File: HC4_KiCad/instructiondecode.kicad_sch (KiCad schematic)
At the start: 57 parts, among them IC10 74HC4002, IC18 74HC32, IC19 74HC74, IC20 74HC00, IC21 74HC4053, IC22 74HC04, IC23 74HC151

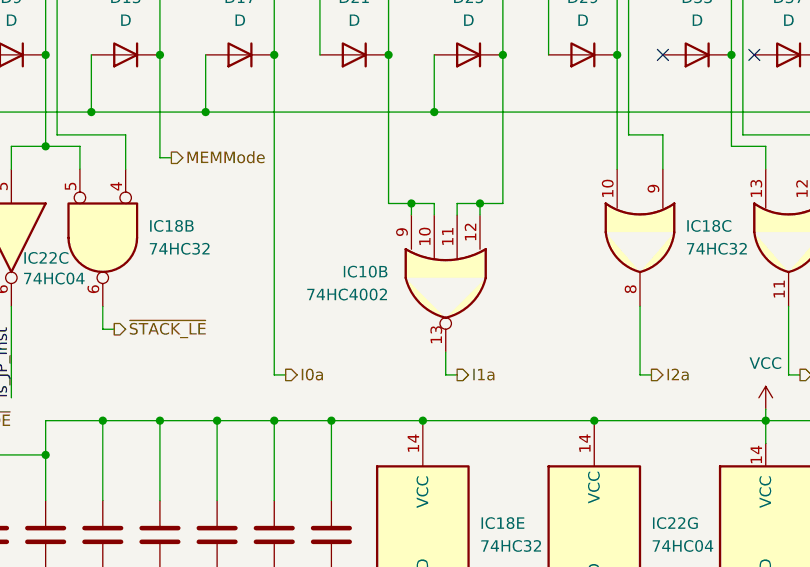
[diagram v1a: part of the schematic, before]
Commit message: とりあえずIC配置確定
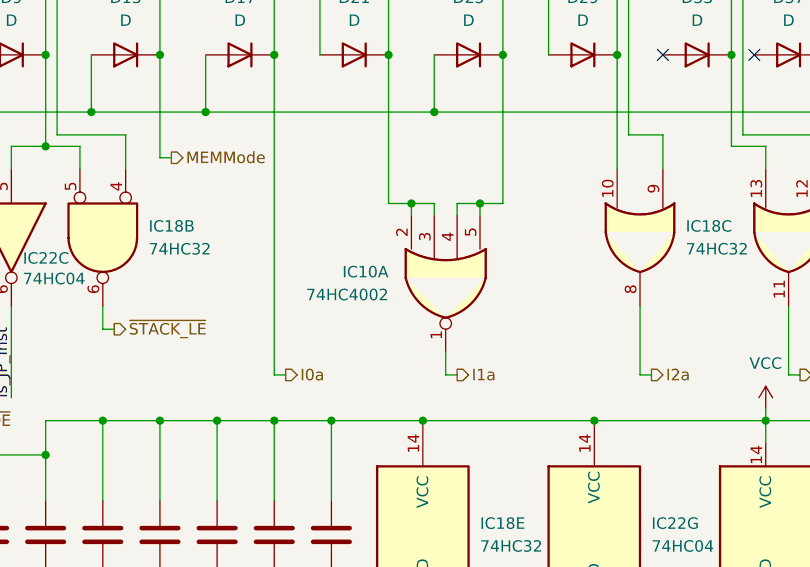
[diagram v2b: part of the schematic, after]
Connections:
- net I1a: now also IC10.1; no longer IC10.13
- net at D18.1 (K), D19.1 (K), D20.1 (K)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: now also IC10.2, IC10.3; no longer IC10.10, IC10.9
- net at D22.1 (K), D23.1 (K), D24.1 (K)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: now also IC10.4, IC10.5; no longer IC10.11, IC10.12
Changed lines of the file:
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@@
 		(at 205.74 120.65 90)
 		(mirror x)
-		(unit 2)
+		(unit 1)
 		(exclude_from_sim no)
 		(in_bom yes)
@@
 				(path "/33731ded-38c0-4297-bdd8-92b082f46ff8/164b1f41-83dc-48ee-8dfe-457b556a7022"
 					(reference "IC10")
-					(unit 2)
+					(unit 1)
 				)
 			)

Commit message: またも手直し
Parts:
- renumbered RN6 to RN8
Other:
- title: CPU -> HC4_CPU

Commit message: 回路の改良　試験は明日やる
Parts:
- removed unit 4 of IC20
- removed unit 3 of IC20
- removed unit 4 of IC22
- removed RN8: 10k, Resistor_THT:R_Array_SIP9, symbol Device:R_Network08_Split
- added unit 4 of IC20
- added unit 3 of IC21
- added unit 4 of IC21
- added RN7: 10k, Resistor_THT:R_Array_SIP9, symbol Device:R_Network08_Split
- D10, D11, D12, D13, D14, D15, D16, D17, D18, D19, D2, D20, D21, D22, D23, D24, D25, D26, D27, D28, D29, D3, D30, D31, D32, D33, D34, D35, D36, D37, D38, D39, D4, D40, D41, D5, D6, D7, D8, D9: footprint Library:DO-35_horizontal_anodeup_Smallhole -> Diode_SMD:D_SOD-323_HandSoldering
- renumbered IC19 to IC18, IC18 to IC19, IC22 to IC20, IC20 to IC21, IC21 to IC22
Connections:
- net ALU_~{Eb}: now also IC21.11
- net I0a: now also D14.2 (A), D15.2 (A), D16.2 (A), D17.2 (A), RN7.5 (R4.2); no longer D14.1 (K), D15.1 (K), D16.1 (K), D17.1 (K)
- net Instruction_0: no longer IC22.10 (B)
- net Instruction_4: now also D21.1 (K), D29.1 (K); no longer D21.2 (A), D29.2 (A)
- net Instruction_5: now also D24.1 (K), D32.1 (K), D4.1 (K), D8.1 (K); no longer D20.2 (A), D24.2 (A), D32.2 (A), D4.2 (A), D8.2 (A)
- net Instruction_6: now also D15.1 (K), D23.1 (K), D31.1 (K), D7.1 (K); no longer D15.2 (A), D23.2 (A), D31.2 (A), D7.2 (A)
- net LevelC_OE: now also D38.2 (A), D39.2 (A), D40.2 (A), D41.2 (A); no longer D38.1 (K), D39.1 (K), D40.1 (K), D41.1 (K)
- net MEMMode: now also D10.2 (A), D11.2 (A), D12.2 (A), D13.2 (A), RN7.4 (R3.2); no longer D10.1 (K), D11.1 (K), D12.1 (K), D13.1 (K)
- net READ: now also D34.2 (A), D35.2 (A), D36.2 (A), D37.2 (A); no longer D34.1 (K), D35.1 (K), D36.1 (K), D37.1 (K)
- net VCC: now also IC20.9, RN7.1 (R1), RN7.1 (R1), RN7.1 (R1), RN7.1 (R1), RN7.1 (R1), RN7.1 (R1), RN7.1 (R1), RN7.1 (R1)
- net ~{ALU_OE}: now also D34.1 (K), D6.1 (K), IC22.10 (B), IC21.10; no longer D2.2 (A), D34.2 (A), D6.2 (A)
- net ~{Imm_OE}: now also IC21.8
- net ~{i4}: now also D13.1 (K), D17.1 (K), D25.1 (K); no longer D13.2 (A), D17.2 (A), D25.2 (A)
- net ~{i5}: now also D12.1 (K), D16.1 (K), D36.1 (K), D40.1 (K); no longer D12.2 (A), D16.2 (A), D36.2 (A), D40.2 (A)
- net ~{i6}: now also D11.1 (K), D19.1 (K), D27.1 (K), D3.1 (K), D35.1 (K), D39.1 (K); no longer D11.2 (A), D19.2 (A), D27.2 (A), D3.2 (A), D35.2 (A), D39.2 (A)
- net ~{i7}: now also IC21.13
- net at D33.2 (A): now also D30.2 (A), D31.2 (A), D32.2 (A), IC19.13, RN7.9 (R8.2)
- net at D26.2 (A): now also D27.2 (A), D28.2 (A), D29.2 (A), IC19.10, RN7.8 (R7.2)
- net at D5.2 (A): now also D2.2 (A), D3.2 (A), D4.2 (A), IC21.12, IC21.9, RN7.2 (R1.2)
- net at D18.2 (A): now also D19.2 (A), D20.2 (A), D21.2 (A), IC10.2, IC10.3, RN7.6 (R5.2)
- net at D22.2 (A): now also D23.2 (A), D24.2 (A), D25.2 (A), IC10.4, IC10.5, RN7.7 (R6.2)
- net at D9.2 (A): now also D6.2 (A), D7.2 (A), D8.2 (A), IC19.5, IC20.5, RN7.3 (R2.2)
- now unconnected: D18.1 (K), D2.1 (K), D20.1 (K), D22.1 (K), D26.1 (K), D28.1 (K), D30.1 (K), D33.1 (K), D5.1 (K), D9.1 (K)
- no-connect marks 19 -> 21
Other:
- moved on the sheet: D10, D11, D12, D13, D14, D15, D16, D17, D18, D19, D2, D20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

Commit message: フットプリントをSOPに変更
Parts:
- CP17, CP18, CP19, CP20, CP21, CP22, CP23: footprint Capacitor_THT:C_Disc_D3.0mm_W1.6mm_P2.50mm -> Capacitor_SMD:C_0603_1608Metric
- IC10, IC18, IC19, IC20, IC21: footprint Package_DIP:DIP-14_W7.62mm_Socket -> Package_SO:SO-14_5.3x10.2mm_P1.27mm
- IC22, IC23: footprint Package_DIP:DIP-16_W7.62mm_Socket -> Package_SO:SO-16_5.3x10.2mm_P1.27mm
- R5, R6: footprint Resistor_THT:R_Axial_DIN0207_L6.3mm_D2.5mm_P7.62mm_Horizontal -> Resistor_SMD:R_0603_1608Metric
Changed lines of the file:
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@@
 			)
 		)
-		(property "Footprint" "Package_DIP:DIP-14_W7.62mm_Socket"
+		(property "Footprint" "Package_SO:SO-14_5.3x10.2mm_P1.27mm"
 			(at 69.85 45.72 0)
 			(effects
@@
 			)
 		)
-		(property "Footprint" "Capacitor_THT:C_Disc_D3.0mm_W1.6mm_P2.50mm"
+		(property "Footprint" "Capacitor_SMD:C_0603_1608Metric"
 			(at 181.3052 152.4 0)
 			(effects
@@
 			)
 		)
-		(property "Footprint" "Package_DIP:DIP-14_W7.62mm_Socket"
+		(property "Footprint" "Package_SO:SO-14_5.3x10.2mm_P1.27mm"
 			(at 118.11 63.5 0)
 			(effects
@@
 			)
 		)
-		(property "Footprint" "Capacitor_THT:C_Disc_D3.0mm_W1.6mm_P2.50mm"
+		(property "Footprint" "Capacitor_SMD:C_0603_1608Metric"
 			(at 187.6552 152.4 0)
 			(effects
@@
 			)
 		)
-		(property "Footprint" "Package_DIP:DIP-14_W7.62mm_Socket"
+		(property "Footprint" "Package_SO:SO-14_5.3x10.2mm_P1.27mm"
 			(at 273.05 148.59 0)
 			(effects
@@
 			)
 		)
-		(property "Footprint" "Package_DIP:DIP-14_W7.62mm_Socket"
+		(property "Footprint" "Package_SO:SO-14_5.3x10.2mm_P1.27mm"
 			(at 104.14 133.35 0)
 			(effects
@@
 			)
 		)
-		(property "Footprint" "Capacitor_THT:C_Disc_D3.0mm_W1.6mm_P2.50mm"
+		(property "Footprint" "Capacitor_SMD:C_0603_1608Metric"
 			(at 168.6052 152.4 0)
 			(effects
@@
 			)
 		)
-		(property "Footprint" "Package_DIP:DIP-14_W7.62mm_Socket"
+		(property "Footprint" "Package_SO:SO-14_5.3x10.2mm_P1.27mm"
 			(at 149.86 121.92 0)
 			(effects
@@
 			)
 		)
-		(property "Footprint" "Package_DIP:DIP-14_W7.62mm_Socket"
+		(property "Footprint" "Package_SO:SO-14_5.3x10.2mm_P1.27mm"
 			(at 261.62 148.59 0)
 			(effects
@@
 			)
 		)
-		(property "Footprint" "Package_DIP:DIP-14_W7.62mm_Socket"
+		(property "Footprint" "Package_SO:SO-14_5.3x10.2mm_P1.27mm"
 			(at 241.3 148.59 0)
 			(effects
@@
 			)
 		)
-		(property "Footprint" "Package_DIP:DIP-14_W7.62mm_Socket"
+		(property "Footprint" "Package_SO:SO-14_5.3x10.2mm_P1.27mm"
 			(at 118.11 82.55 0)
 			(effects
@@
 			)
 		)
-		(property "Footprint" "Package_DIP:DIP-14_W7.62mm_Socket"
+		(property "Footprint" "Package_SO:SO-14_5.3x10.2mm_P1.27mm"
 			(at 118.11 101.6 0)
 			(effects
@@
 			)
 		)
-		(property "Footprint" "Package_DIP:DIP-16_W7.62mm_Socket"
+		(property "Footprint" "Package_SO:SO-16_5.3x10.2mm_P1.27mm"
 			(at 130.81 163.83 0)
 			(effects
@@
 			)
 		)
-		(property "Footprint" "Package_DIP:DIP-14_W7.62mm_Socket"
+		(property "Footprint" "Package_SO:SO-14_5.3x10.2mm_P1.27mm"
 			(at 29.21 143.51 0)
 			(effects
@@
 			)
 		)
-		(property "Footprint" "Package_DIP:DIP-14_W7.62mm_Socket"
+		(property "Footprint" "Package_SO:SO-14_5.3x10.2mm_P1.27mm"
 			(at 243.84 115.57 0)
 			(effects
@@
 			)
 		)
-		(property "Footprint" "Package_DIP:DIP-14_W7.62mm_Socket"
+		(property "Footprint" "Package_SO:SO-14_5.3x10.2mm_P1.27mm"
 			(at 139.7 121.92 0)
 			(effects
@@
 			)
 		)
-		(property "Footprint" "Package_DIP:DIP-14_W7.62mm_Socket"
+		(property "Footprint" "Package_SO:SO-14_5.3x10.2mm_P1.27mm"
 			(at 170.18 115.57 0)
 			(effects
@@
 			)
 		)
-		(property "Footprint" "Package_DIP:DIP-14_W7.62mm_Socket"
+		(property "Footprint" "Package_SO:SO-14_5.3x10.2mm_P1.27mm"
 			(at 118.11 44.45 0)
 			(effects
@@
 			)
 		)
-		(property "Footprint" "Package_DIP:DIP-14_W7.62mm_Socket"
+		(property "Footprint" "Package_SO:SO-14_5.3x10.2mm_P1.27mm"
 			(at 40.64 92.71 0)
 			(effects
@@
 			)
 		)
-		(property "Footprint" "Package_DIP:DIP-14_W7.62mm_Socket"
+		(property "Footprint" "Package_SO:SO-14_5.3x10.2mm_P1.27mm"
 			(at 67.31 92.71 0)
 			(effects
@@
 			)
 		)
-		(property "Footprint" "Package_DIP:DIP-14_W7.62mm_Socket"
+		(property "Footprint" "Package_SO:SO-14_5.3x10.2mm_P1.27mm"
 			(at 205.74 120.65 0)
 			(effects
@@
 			)
 		)
-		(property "Footprint" "Package_DIP:DIP-14_W7.62mm_Socket"
+		(property "Footprint" "Package_SO:SO-14_5.3x10.2mm_P1.27mm"
 			(at 227.33 115.57 0)
 			(effects
@@
 			)
 		)
-		(property "Footprint" "Package_DIP:DIP-16_W7.62mm_Socket"
+		(property "Footprint" "Package_SO:SO-16_5.3x10.2mm_P1.27mm"
 			(at 73.66 147.32 0)
 			(effects
@@
 			)
 		)
-		(property "Footprint" "Package_DIP:DIP-14_W7.62mm_Socket"
+		(property "Footprint" "Package_SO:SO-14_5.3x10.2mm_P1.27mm"
 			(at 222.25 148.59 0)
 			(effects
@@
 			)
 		)
-		(property "Footprint" "Capacitor_THT:C_Disc_D3.0mm_W1.6mm_P2.50mm"
+		(property "Footprint" "Capacitor_SMD:C_0603_1608Metric"
 			(at 174.9552 152.4 0)
 			(effects
@@
 			)
 		)
-		(property "Footprint" "Resistor_THT:R_Axial_DIN0207_L6.3mm_D2.5mm_P7.62mm_Horizontal"
+		(property "Footprint" "Resistor_SMD:R_0603_1608Metric"
 			(at 259.842 20.32 90)
 			(effects
@@
 			)
 		)
-		(property "Footprint" "Package_DIP:DIP-14_W7.62mm_Socket"
+		(property "Footprint" "Package_SO:SO-14_5.3x10.2mm_P1.27mm"
 			(at 158.75 115.57 0)
 			(effects
@@
 			)
 		)
-		(property "Footprint" "Capacitor_THT:C_Disc_D3.0mm_W1.6mm_P2.50mm"
+		(property "Footprint" "Capacitor_SMD:C_0603_1608Metric"
 			(at 194.0052 152.4 0)
 			(effects
@@
 			)
 		)
-		(property "Footprint" "Capacitor_THT:C_Disc_D3.0mm_W1.6mm_P2.50mm"
+		(property "Footprint" "Capacitor_SMD:C_0603_1608Metric"
 			(at 162.2552 152.4 0)
 			(effects
@@
 			)
 		)
-		(property "Footprint" "Package_DIP:DIP-14_W7.62mm_Socket"
+		(property "Footprint" "Package_SO:SO-14_5.3x10.2mm_P1.27mm"
 			(at 69.85 60.96 0)
 			(effects
@@
 			)
 		)
-		(property "Footprint" "Capacitor_THT:C_Disc_D3.0mm_W1.6mm_P2.50mm"
+		(property "Footprint" "Capacitor_SMD:C_0603_1608Metric"
 			(at 155.9052 152.4 0)
 			(effects
@@
 			)
 		)
-		(property "Footprint" "Package_DIP:DIP-14_W7.62mm_Socket"
+		(property "Footprint" "Package_SO:SO-14_5.3x10.2mm_P1.27mm"
 			(at 203.2 148.59 0)
 			(effects
@@
 			)
 		)
-		(property "Footprint" "Resistor_THT:R_Axial_DIN0207_L6.3mm_D2.5mm_P7.62mm_Horizontal"
+		(property "Footprint" "Resistor_SMD:R_0603_1608Metric"
 			(at 245.872 20.32 90)
 			(effects

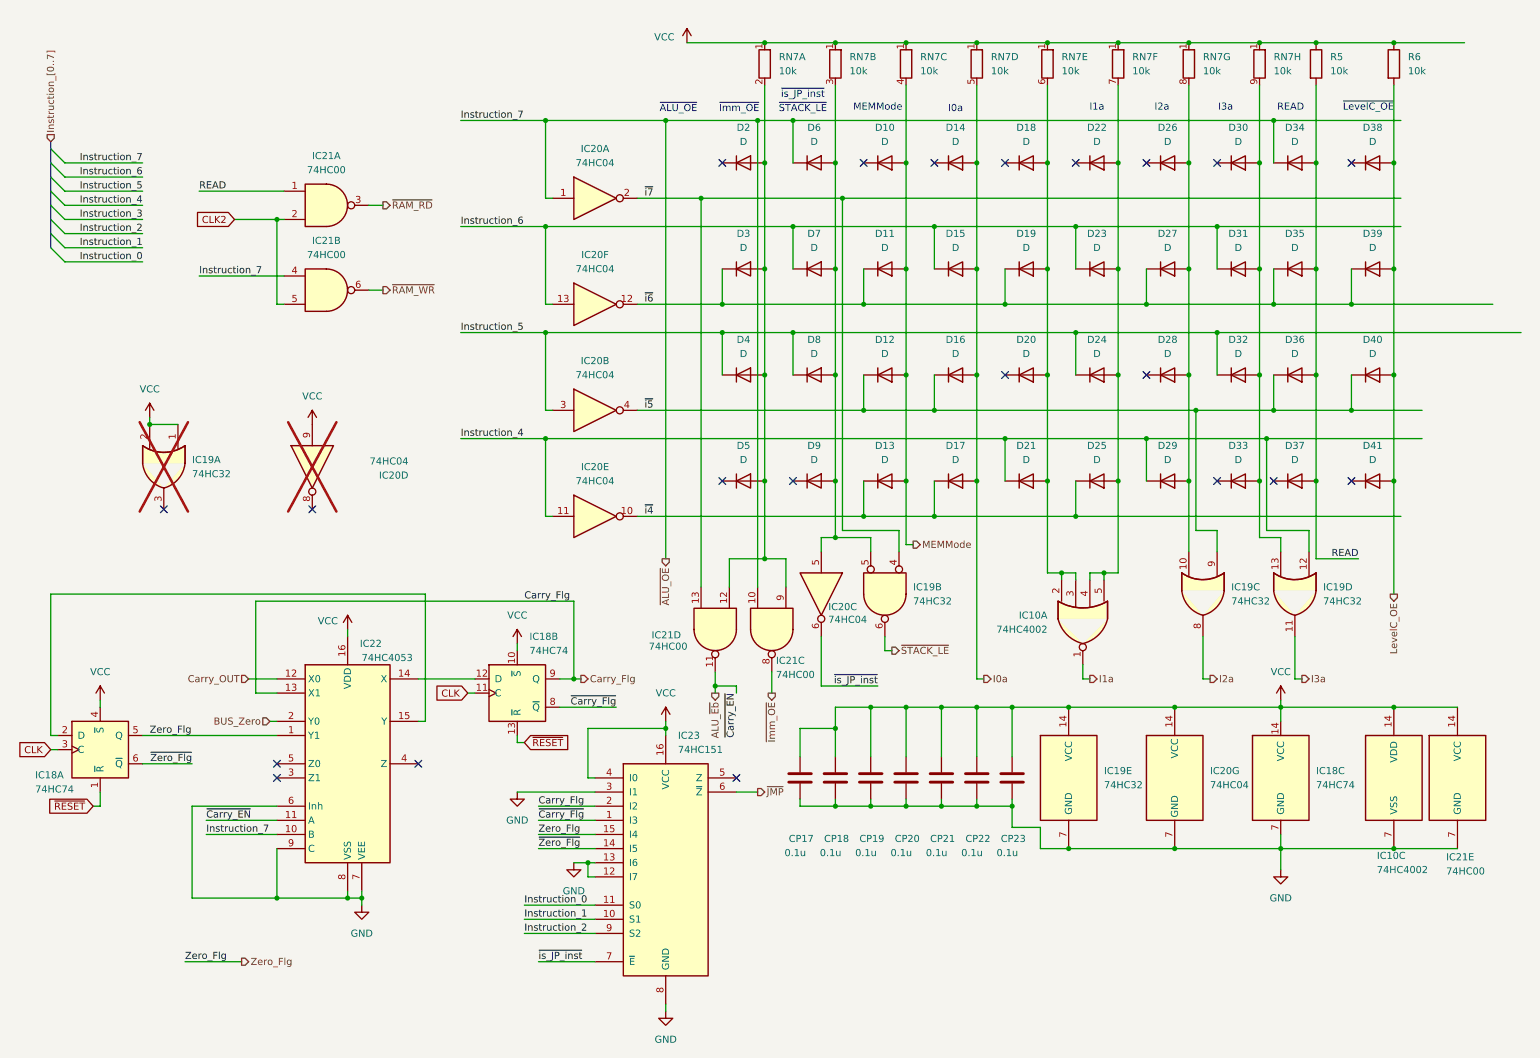
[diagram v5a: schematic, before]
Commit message: Spiceのファイルを追加
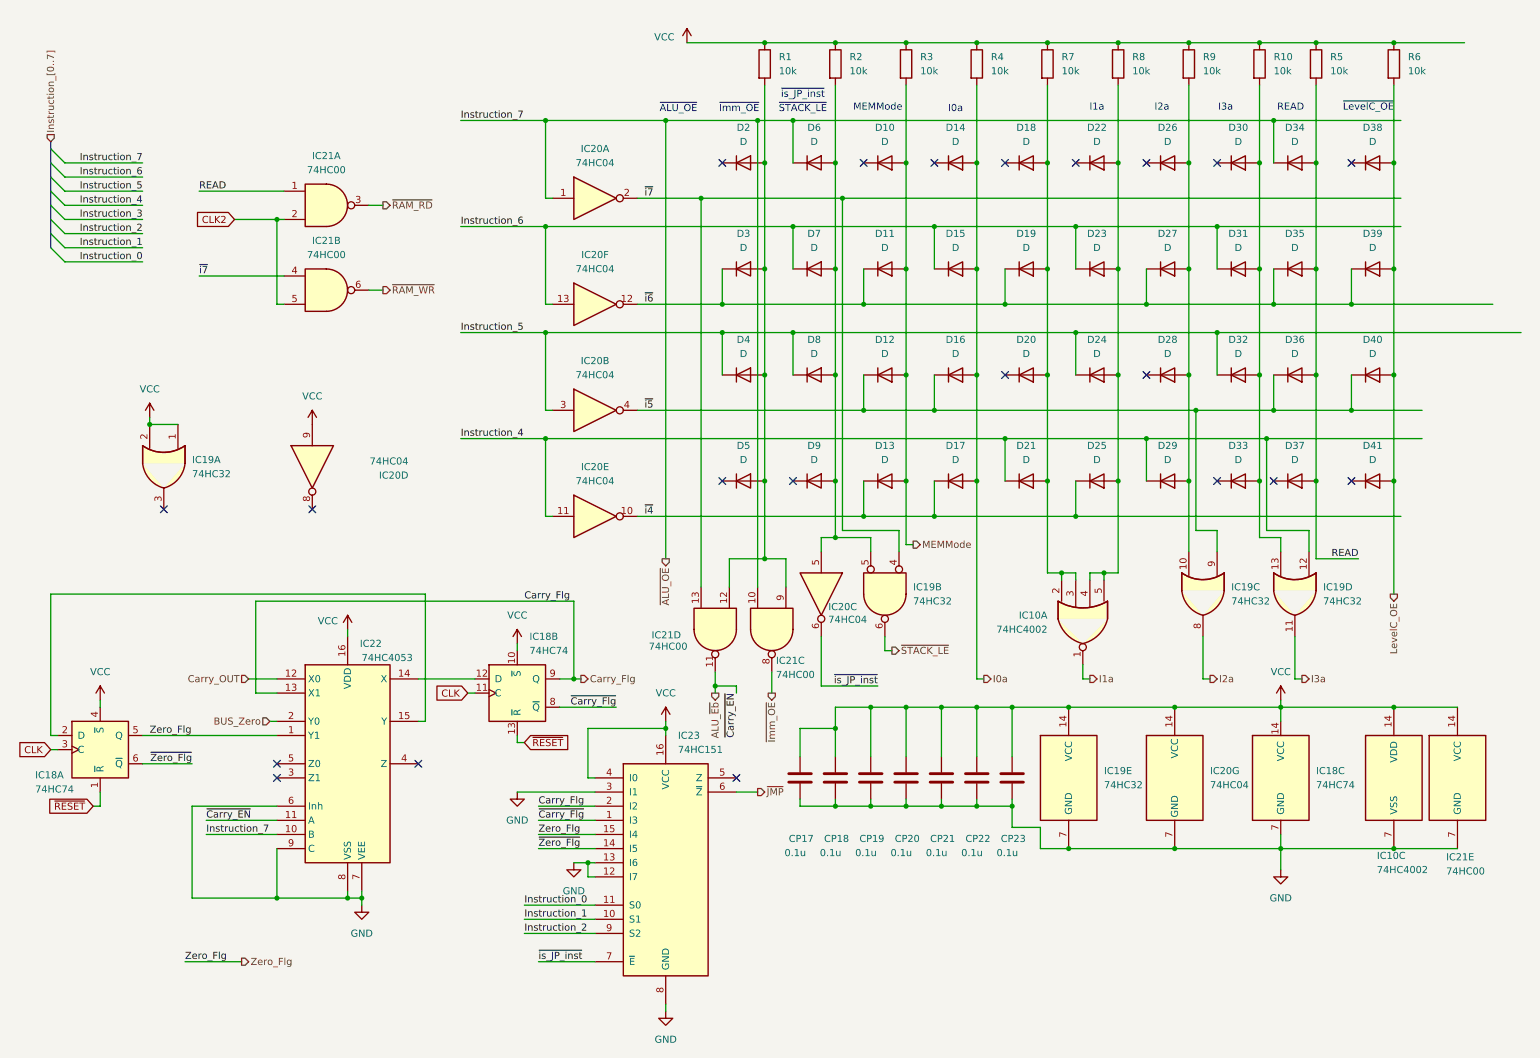
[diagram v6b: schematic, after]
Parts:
- removed RN7: 10k, Resistor_THT:R_Array_SIP9, symbol Device:R_Network08_Split
- added R1, R10, R2, R3, R4, R7, R8, R9: 10k, Resistor_SMD:R_0603_1608Metric, symbol Device:R
- IC19, IC20: now fitted
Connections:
- net I0a: now also R4.2
- net MEMMode: now also R3.2
- net VCC: now also R1.1, R10.1, R2.1, R3.1, R4.1, R7.1, R8.1, R9.1
- net ~{ALU_OE}: no longer IC21.4
- net ~{i7}: now also IC21.4
- net at D26.2 (A), D27.2 (A), D28.2 (A)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: now also R9.2
- net at D30.2 (A), D31.2 (A), D32.2 (A)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: now also R10.2
- net at D2.2 (A), D3.2 (A), D4.2 (A)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: now also R1.2
- net at D6.2 (A), D7.2 (A), D8.2 (A)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: now also R2.2
- net at D18.2 (A), D19.2 (A), D20.2 (A)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: now also R7.2
- net at D22.2 (A), D23.2 (A), D24.2 (A)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: now also R8.2

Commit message: 基板ぬ
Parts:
- renumbered R8 to R10, R9 to R11, R10 to R12, R5 to R13, R6 to R14, R1 to R5, R2 to R6, R3 to R7, R4 to R8, R7 to R9

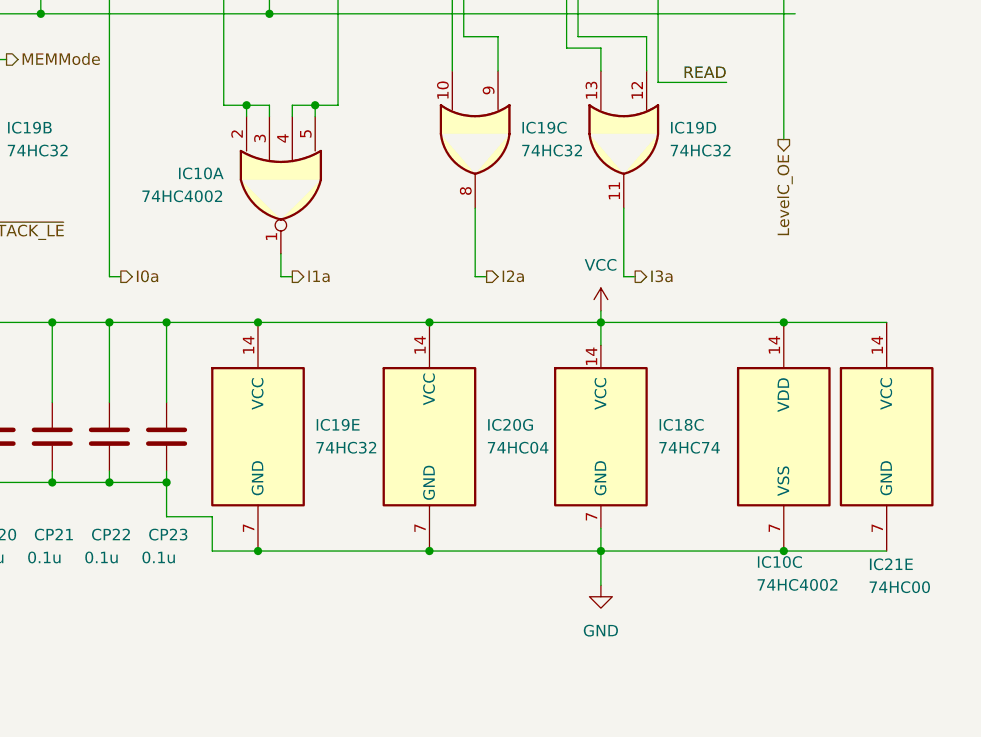
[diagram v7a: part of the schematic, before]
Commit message: Added output port for blink
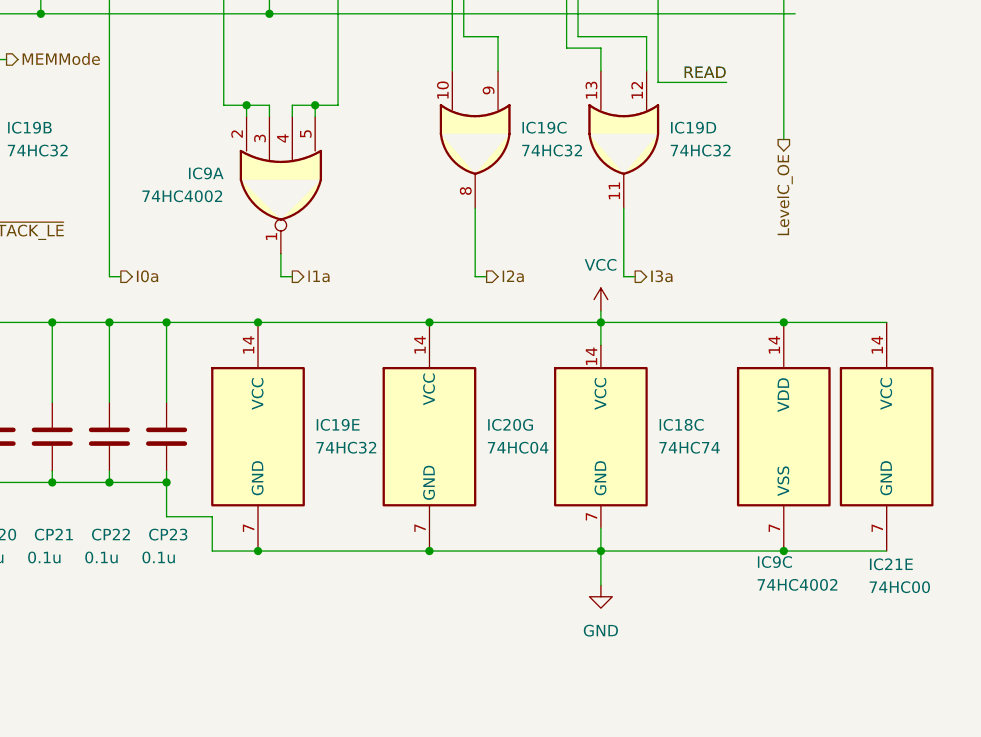
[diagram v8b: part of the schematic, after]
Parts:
- renumbered IC10 to IC9
